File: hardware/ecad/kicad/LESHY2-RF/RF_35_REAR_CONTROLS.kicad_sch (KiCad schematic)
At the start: 0 parts

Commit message: complete exact H2.3.1 RF power hierarchy
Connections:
- no-connect marks 0 -> 6
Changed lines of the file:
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@@
 	(generator_version "10.0")
 	(paper "A4")
+	(hierarchical_label "3V3_MAIN"
+		(shape bidirectional)
+		(at 20.32 20.32 0)
+		(effects (font (size 1.27 1.27)))
+	)
+	(wire
+		(pts (xy 20.32 20.32) (xy 25.40 20.32))
+		(stroke (width 0) (type default))
+	)
+	(no_connect (at 25.40 20.32)
+	)
+	(hierarchical_label "ENCODER_A"
+		(shape bidirectional)
+		(at 20.32 25.40 0)
+		(effects (font (size 1.27 1.27)))
+	)
+	(wire
+		(pts (xy 20.32 25.40) (xy 25.40 25.40))
+		(stroke (width 0) (type default))
+	)
+	(no_connect (at 25.40 25.40)
+	)
+	(hierarchical_label "ENCODER_B"
+		(shape bidirectional)
+		(at 20.32 30.48 0)
+		(effects (font (size 1.27 1.27)))
+	)
+	(wire
+		(pts (xy 20.32 30.48) (xy 25.40 30.48))
+		(stroke (width 0) (type default))
+	)
+	(no_connect (at 25.40 30.48)
+	)
+	(hierarchical_label "POWER_GROUND"
+		(shape bidirectional)
+		(at 190.50 20.32 180)
+		(effects (font (size 1.27 1.27)) (justify right))
+	)
+	(wire
+		(pts (xy 190.50 20.32) (xy 185.42 20.32))
+		(stroke (width 0) (type default))
+	)
+	(no_connect (at 185.42 20.32)
+	)
+	(hierarchical_label "PTT_BUTTON_N"
+		(shape bidirectional)
+		(at 190.50 25.40 180)
+		(effects (font (size 1.27 1.27)) (justify right))
+	)
+	(wire
+		(pts (xy 190.50 25.40) (xy 185.42 25.40))
+		(stroke (width 0) (type default))
+	)
+	(no_connect (at 185.42 25.40)
+	)
+	(hierarchical_label "UI_ENCODER_PUSH_N"
+		(shape bidirectional)
+		(at 190.50 30.48 180)
+		(effects (font (size 1.27 1.27)) (justify right))
+	)
+	(wire
+		(pts (xy 190.50 30.48) (xy 185.42 30.48))
+		(stroke (width 0) (type default))
+	)
+	(no_connect (at 185.42 30.48)
+	)
 	(sheet_instances
 		(path "/"

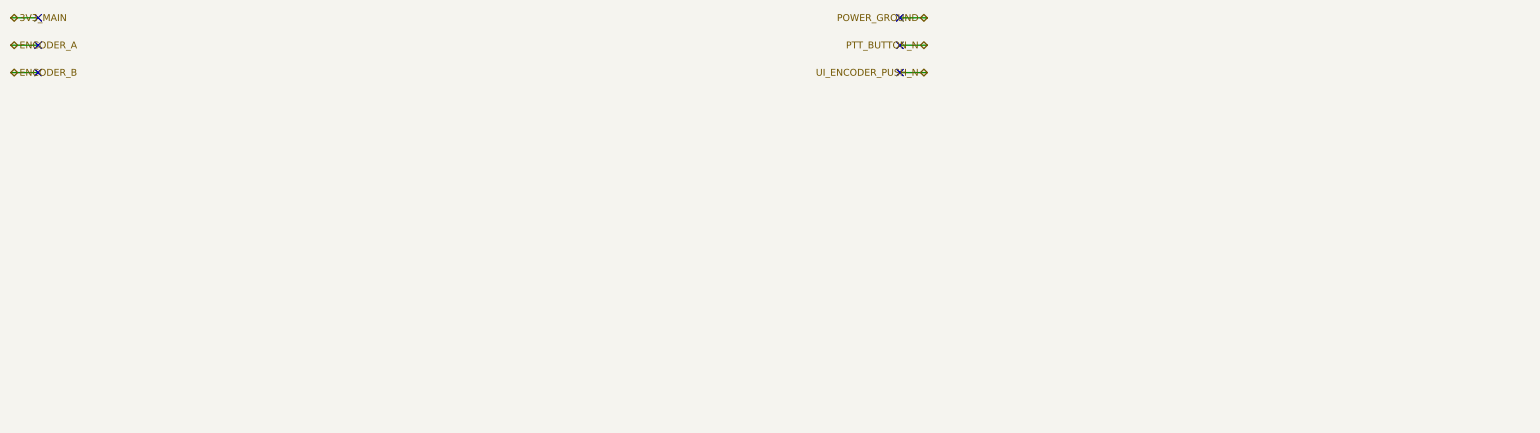
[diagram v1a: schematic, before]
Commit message: complete exact H2.3.9 rear controls sheet
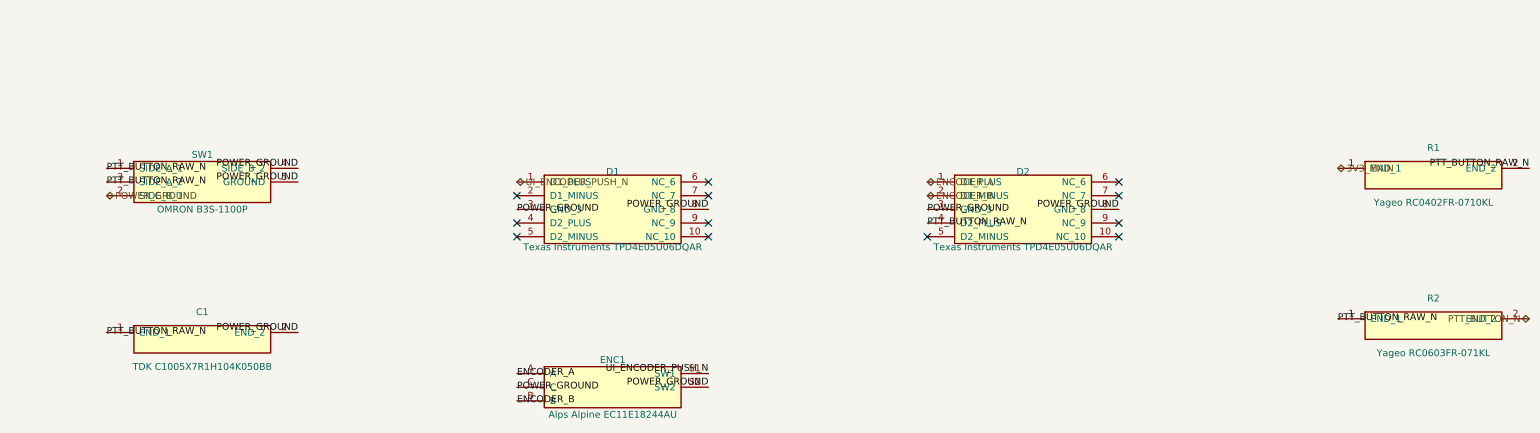
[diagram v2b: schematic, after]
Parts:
- added C1: TDK C1005X7R1H104K050BB, Capacitor_SMD:C_0402_1005Metric, symbol Leshy2:RF35_PTT_FILTER_CAP
- added D1: Texas Instruments TPD4E05U06DQAR, Package_SON:USON-10_2.5x1.0mm_P0.5mm, symbol Leshy2:RF35_REAR_CONTROL_ESD
- added D2: Texas Instruments TPD4E05U06DQAR, Package_SON:USON-10_2.5x1.0mm_P0.5mm, symbol Leshy2:RF35_ENCODER_PTT_ESD
- added ENC1: Alps Alpine EC11E18244AU, Rotary_Encoder:RotaryEncoder_Alps_EC11E-Switch_Vertical_H20mm_MountingHoles, symbol Leshy2:RF35_ENCODER
- added R1: Yageo RC0402FR-0710KL, Resistor_SMD:R_0402_1005Metric, symbol Leshy2:RF35_PTT_PULLUP
- added R2: Yageo RC0603FR-071KL, Resistor_SMD:R_0603_1608Metric, symbol Leshy2:RF35_PTT_SERIES
- added SW1: OMRON B3S-1100P, Leshy2:B3S-1100P, symbol Leshy2:RF35_PTT_SWITCH
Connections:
- net 3V3_MAIN: now also R1.1 (END_1)
- net ENCODER_A: now also D2.1 (D1_PLUS), ENC1.A
- net ENCODER_B: now also D2.2 (D1_MINUS), ENC1.B
- net POWER_GROUND: now also C1.2 (END_2), D1.3 (GND_3), D1.8 (GND_8), D2.3 (GND_3), D2.8 (GND_8), ENC1.C, ENC1.S2 (SW2), SW1.2 (SIDE_B_1), SW1.4 (SIDE_B_2), SW1.5 (GROUND)
- net PTT_BUTTON_N: now also R2.2 (END_2)
- net UI_ENCODER_PUSH_N: now also D1.1 (D1_PLUS), ENC1.S1 (SW1)
- new net PTT_BUTTON_RAW_N: C1.1 (END_1), D2.4 (D2_PLUS), R1.2 (END_2), R2.1 (END_1), SW1.1 (SIDE_A_1), SW1.3 (SIDE_A_2)
- no-connect marks 6 -> 12
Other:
- title: (none) -> Leshy2 — rear encoder, push and independent PTT

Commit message: complete H2 schematic review package
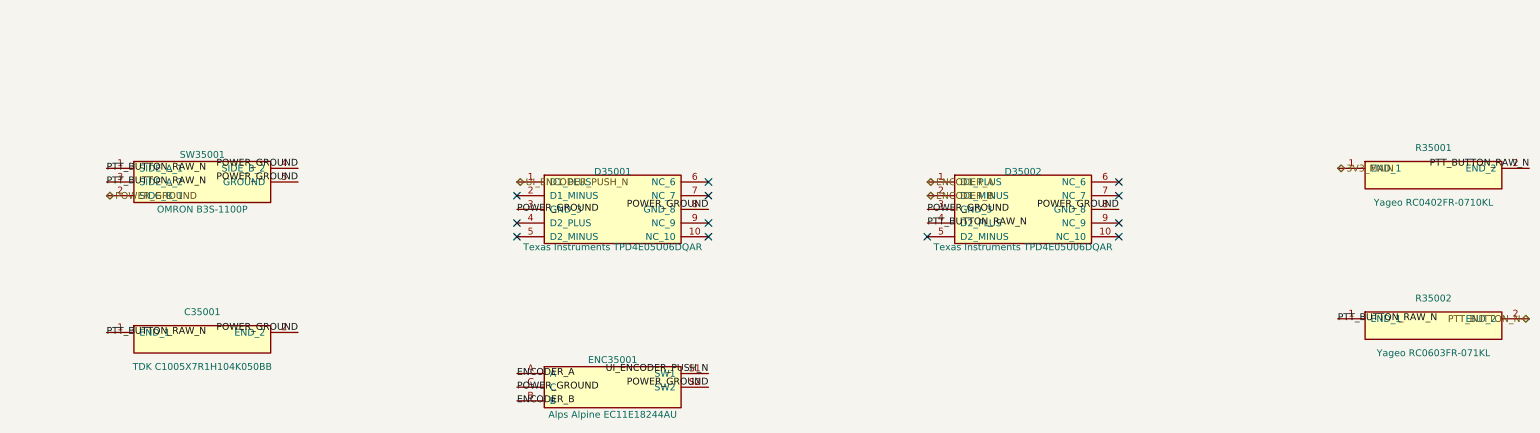
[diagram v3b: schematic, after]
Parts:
- renumbered C1 to C35001, D1 to D35001, D2 to D35002, ENC1 to ENC35001, R1 to R35001, R2 to R35002, SW1 to SW35001
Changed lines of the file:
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@@
 		(on_board yes)
 		(dnp no)
-		(property "Reference" "SW1"
+		(property "Reference" "SW35001"
 			(at 55.88 45.72 0)
 			(show_name no)
@@
 			(project "LESHY2-RF"
 				(path "/69fd3e5f-3c69-58f0-b449-24712149534c"
-					(reference "SW1")
+					(reference "SW35001")
 					(unit 1)
 				)
@@
 		(on_board yes)
 		(dnp no)
-		(property "Reference" "D1"
+		(property "Reference" "D35001"
 			(at 132.08 48.88 0)
 			(show_name no)
@@
 			(project "LESHY2-RF"
 				(path "/69fd3e5f-3c69-58f0-b449-24712149534c"
-					(reference "D1")
+					(reference "D35001")
 					(unit 1)
 				)
@@
 		(on_board yes)
 		(dnp no)
-		(property "Reference" "D2"
+		(property "Reference" "D35002"
 			(at 208.28 48.88 0)
 			(show_name no)
@@
 			(project "LESHY2-RF"
 				(path "/69fd3e5f-3c69-58f0-b449-24712149534c"
-					(reference "D2")
+					(reference "D35002")
 					(unit 1)
 				)
@@
 		(on_board yes)
 		(dnp no)
-		(property "Reference" "R1"
+		(property "Reference" "R35001"
 			(at 284.48 44.45 0)
 			(show_name no)
@@
 			(project "LESHY2-RF"
 				(path "/69fd3e5f-3c69-58f0-b449-24712149534c"
-					(reference "R1")
+					(reference "R35001")
 					(unit 1)
 				)
@@
 		(on_board yes)
 		(dnp no)
-		(property "Reference" "R2"
+		(property "Reference" "R35002"
 			(at 284.48 72.39 0)
 			(show_name no)
@@
 			(project "LESHY2-RF"
 				(path "/69fd3e5f-3c69-58f0-b449-24712149534c"
-					(reference "R2")
+					(reference "R35002")
 					(unit 1)
 				)
@@
 		(on_board yes)
 		(dnp no)
-		(property "Reference" "C1"
+		(property "Reference" "C35001"
 			(at 55.88 74.93 0)
 			(show_name no)
@@
 			(project "LESHY2-RF"
 				(path "/69fd3e5f-3c69-58f0-b449-24712149534c"
-					(reference "C1")
+					(reference "C35001")
 					(unit 1)
 				)
@@
 		(on_board yes)
 		(dnp no)
-		(property "Reference" "ENC1"
+		(property "Reference" "ENC35001"
 			(at 132.08 83.82 0)
 			(show_name no)
@@
 			(project "LESHY2-RF"
 				(path "/69fd3e5f-3c69-58f0-b449-24712149534c"
-					(reference "ENC1")
-					(unit 1)
-				)
+					(reference "ENC35001")
+					(unit 1)
+				)

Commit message: Optimize H1 display and stocked BOM routes
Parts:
- C35001: value TDK C1005X7R1H104K050BB -> Yageo CC0402KRX7R9BB104
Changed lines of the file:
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@@
 			(effects (font (size 1.27 1.27)))
 		)
-		(property "Value" "TDK C1005X7R1H104K050BB"
+		(property "Value" "Yageo CC0402KRX7R9BB104"
 			(at 55.88 85.09 0)
 			(show_name no)
